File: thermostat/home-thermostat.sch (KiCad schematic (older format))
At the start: 38 parts, among them J1 Thermosthat, U3 LM2574M-5, U4 LD1117S33TR_SOT223, U5 AT24C512

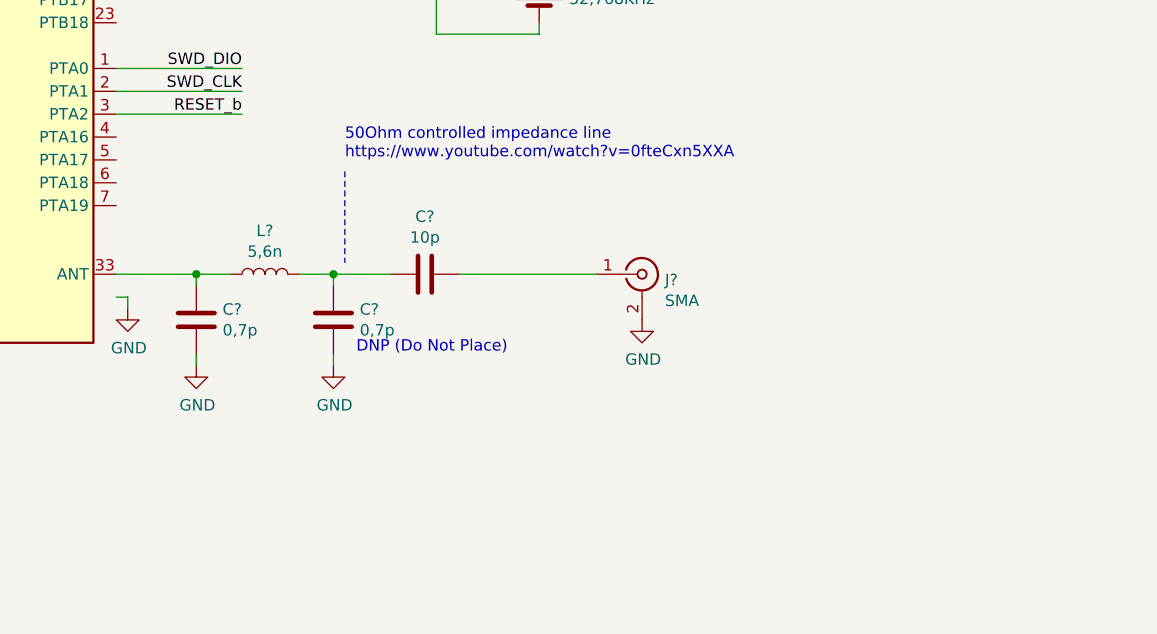
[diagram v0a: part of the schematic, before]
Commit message: Added some helpful comments to schematic, added explanation document to schematic of evalboard.
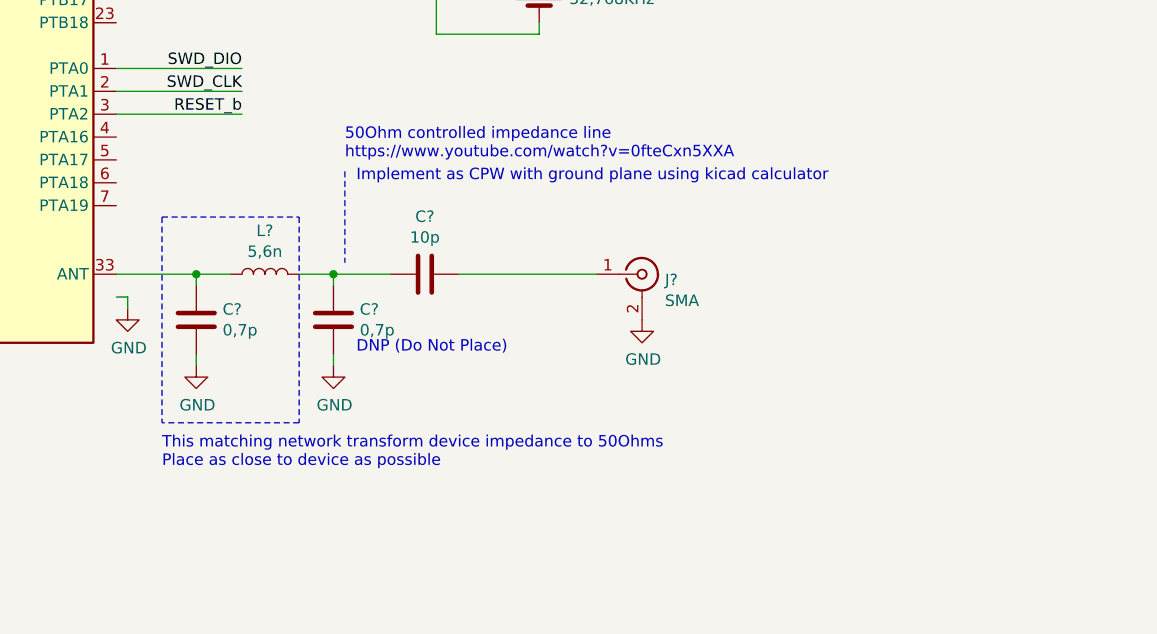
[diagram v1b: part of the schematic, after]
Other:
- note added: "Implement as CPW with ground plane using kicad calculator"
- note added: "This matching network transform device impedance to 50Ohms\nPlace as close to device as possible"
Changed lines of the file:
@@
 Wire Wire Line
 	7700 3800 8150 3800
+Text Notes 7350 4450 0    50   ~ 0
+Implement as CPW with ground plane using kicad calculator
+Wire Notes Line
+	6500 4600 7100 4600
+Wire Notes Line
+	7100 4600 7100 5500
+Wire Notes Line
+	7100 5500 6500 5500
+Wire Notes Line
+	6500 4600 6500 5500
+Text Notes 6500 5700 0    50   ~ 0
+This matching network transform device impedance to 50Ohms\nPlace as close to device as possible
 $EndSCHEMATC

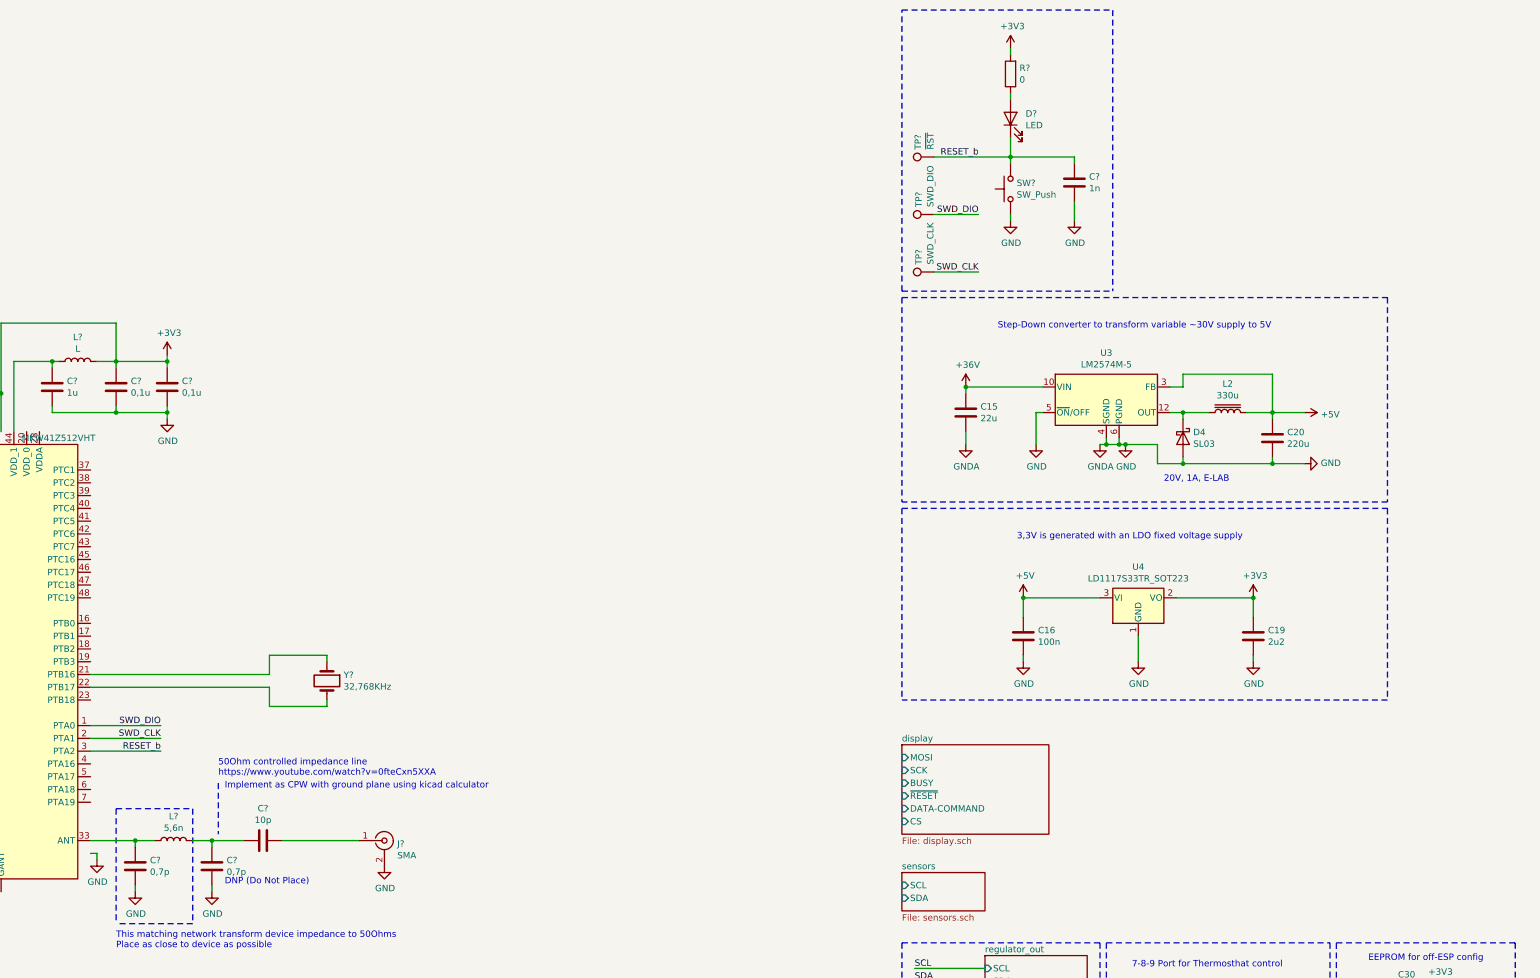
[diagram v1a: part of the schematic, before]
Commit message: Added some comments to pin usage on MKW41Z, reconfigured display to use 3 line SPI (no Data/Command pin) with 9 bit data packets
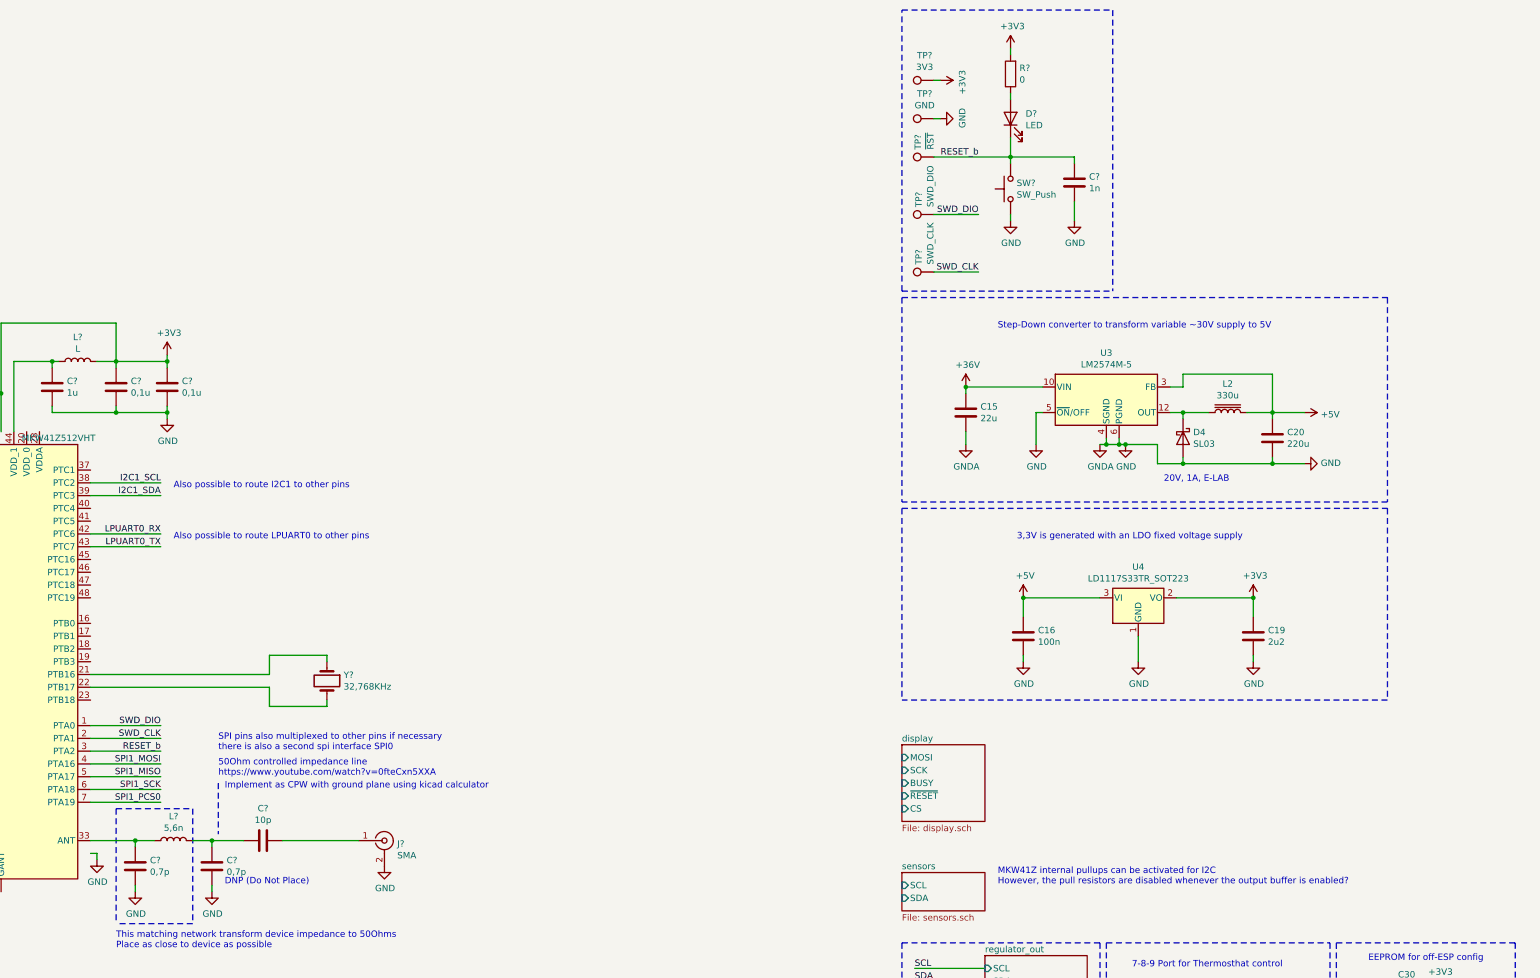
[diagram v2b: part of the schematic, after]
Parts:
- added TP?: GND, symbol Connector:TestPoint
- added TP?: 3V3, symbol Connector:TestPoint
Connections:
- net labels added: I2C1_SCL, I2C1_SDA, LPUART0_RX, LPUART0_TX, SPI1_MISO, SPI1_MOSI, SPI1_PCS0, SPI1_SCK
- wire segments 172 -> 182
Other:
- note added: "Also possible to route I2C1 to other pins"
- note added: "Also possible to route LPUART0 to other pins"
- note added: "MKW41Z internal pullups can be activated for I2C\nHowever, the pull resistors are disabled whenever the output buffer is enabled?"
- note added: "SPI pins also multiplexed to other pins if necessary\nthere is also a second spi interface SPI0"
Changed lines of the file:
@@
 Will we do peripherals with AVR or does MKW41Z has enough free pins?\nDo we want to try touch interface with MKW41 or AVR?
 $Sheet
-S 12650 4100 1150 700
+S 12650 4100 650  600
 U 5F306ECC
 F0 "display" 50
@@
 F4 "BUSY" I L 12650 4400 50
 F5 "~RESET" I L 12650 4500 50
-F6 "DATA-COMMAND" I L 12650 4600 50
-F7 "CS" I L 12650 4700 50
+F6 "CS" I L 12650 4600 50
 $EndSheet
 $Sheet
@@
 Text Notes 6500 5700 0    50   ~ 0
 This matching network transform device impedance to 50Ohms\nPlace as close to device as possible
+$Comp
+L Connector:TestPoint TP?
+U 1 1 5F554204
+P 12900 -800
+F 0 "TP?" V 13095 -728 50  0000 C CNN
+F 1 "GND" V 13004 -728 50  0000 C CNN
+F 2 "" H 13100 -800 50  0001 C CNN
+F 3 "~" H 13100 -800 50  0001 C CNN
+	1    12900 -800
+	0    -1   -1   0
+$EndComp
+$Comp
+L power:GND #PWR?
+U 1 1 5F5544E3
+P 12950 -800
+AR Path="/5E8AC4D3/5F5544E3" Ref="#PWR?"  Part="1"
+AR Path="/5F5544E3" Ref="#PWR?"  Part="1"
+F 0 "#PWR?" H 12950 -1050 50  0001 C CNN
+F 1 "GND" H 12955 -973 50  0000 C CNN
+F 2 "" H 12950 -800 50  0001 C CNN
+F 3 "" H 12950 -800 50  0001 C CNN
+	1    12950 -800
+	0    -1   -1   0
+$EndComp
+Wire Wire Line
+	12950 -800 12900 -800
+$Comp
+L power:+3V3 #PWR?
+U 1 1 5F55E07F
+P 12950 -1100
+AR Path="/5E8AC4D3/5F55E07F" Ref="#PWR?"  Part="1"
+AR Path="/5F55E07F" Ref="#PWR?"  Part="1"
+F 0 "#PWR?" H 12950 -1250 50  0001 C CNN
+F 1 "+3V3" H 12965 -927 50  0000 C CNN
+F 2 "" H 12950 -1100 50  0001 C CNN
+F 3 "" H 12950 -1100 50  0001 C CNN
+	1    12950 -1100
+	0    1    1    0
+$EndComp
+$Comp
+L Connector:TestPoint TP?
+U 1 1 5F55EE65
+P 12900 -1100
+F 0 "TP?" V 13095 -1028 50  0000 C CNN
+F 1 "3V3" V 13004 -1028 50  0000 C CNN
+F 2 "" H 13100 -1100 50  0001 C CNN
+F 3 "~" H 13100 -1100 50  0001 C CNN
+	1    12900 -1100
+	0    -1   -1   0
+$EndComp
+Wire Wire Line
+	12900 -1100 12950 -1100
+Text Label 6850 4250 2    50   ~ 0
+SPI1_MOSI
+Text Label 6850 4350 2    50   ~ 0
+SPI1_MISO
+Text Label 6850 4450 2    50   ~ 0
+SPI1_SCK
+Text Label 6850 4550 2    50   ~ 0
+SPI1_PCS0
+Wire Wire Line
+	6850 4250 6300 4250
+Wire Wire Line
+	6850 4350 6300 4350
+Wire Wire Line
+	6850 4450 6300 4450
+Wire Wire Line
+	6850 4550 6300 4550
+Text Notes 7300 4150 0    50   ~ 0
+SPI pins also multiplexed to other pins if necessary\nthere is also a second spi interface SPI0
+Text Notes 13400 5200 0    50   ~ 0
+MKW41Z internal pullups can be activated for I2C\nHowever, the pull resistors are disabled whenever the output buffer is enabled?
+Text Label 6850 2050 2    50   ~ 0
+I2C1_SCL
+Text Label 6850 2150 2    50   ~ 0
+I2C1_SDA
+Wire Wire Line
+	6850 2050 6300 2050
+Wire Wire Line
+	6850 2150 6300 2150
+Text Notes 6950 2100 0    50   ~ 0
+Also possible to route I2C1 to other pins
+Text Label 6850 2450 2    50   ~ 0
+LPUART0_RX
+Wire Wire Line
+	6850 2450 6300 2450
+Text Label 6850 2550 2    50   ~ 0
+LPUART0_TX
+Wire Wire Line
+	6850 2550 6300 2550
+Text Notes 6950 2500 0    50   ~ 0
+Also possible to route LPUART0 to other pins
 $EndSCHEMATC

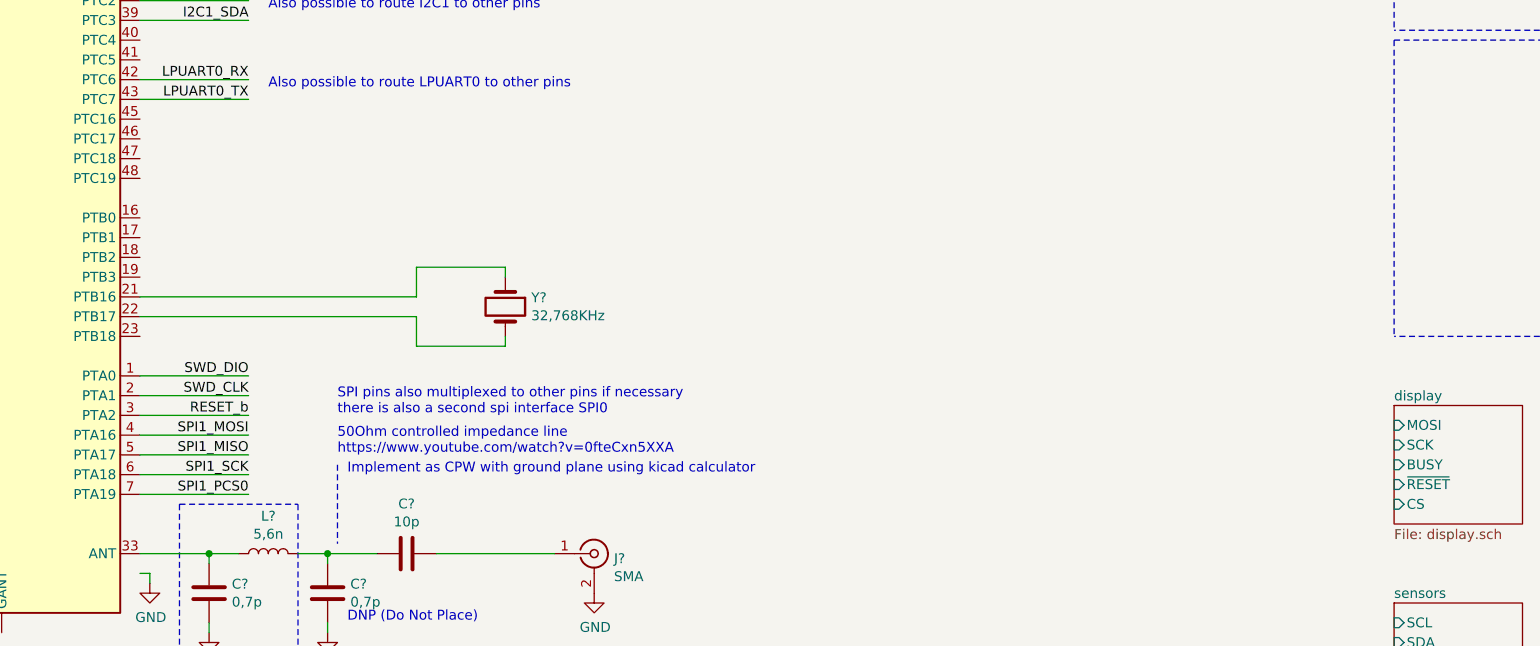
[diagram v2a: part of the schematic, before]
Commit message: Connected display SPI to MKW41Z
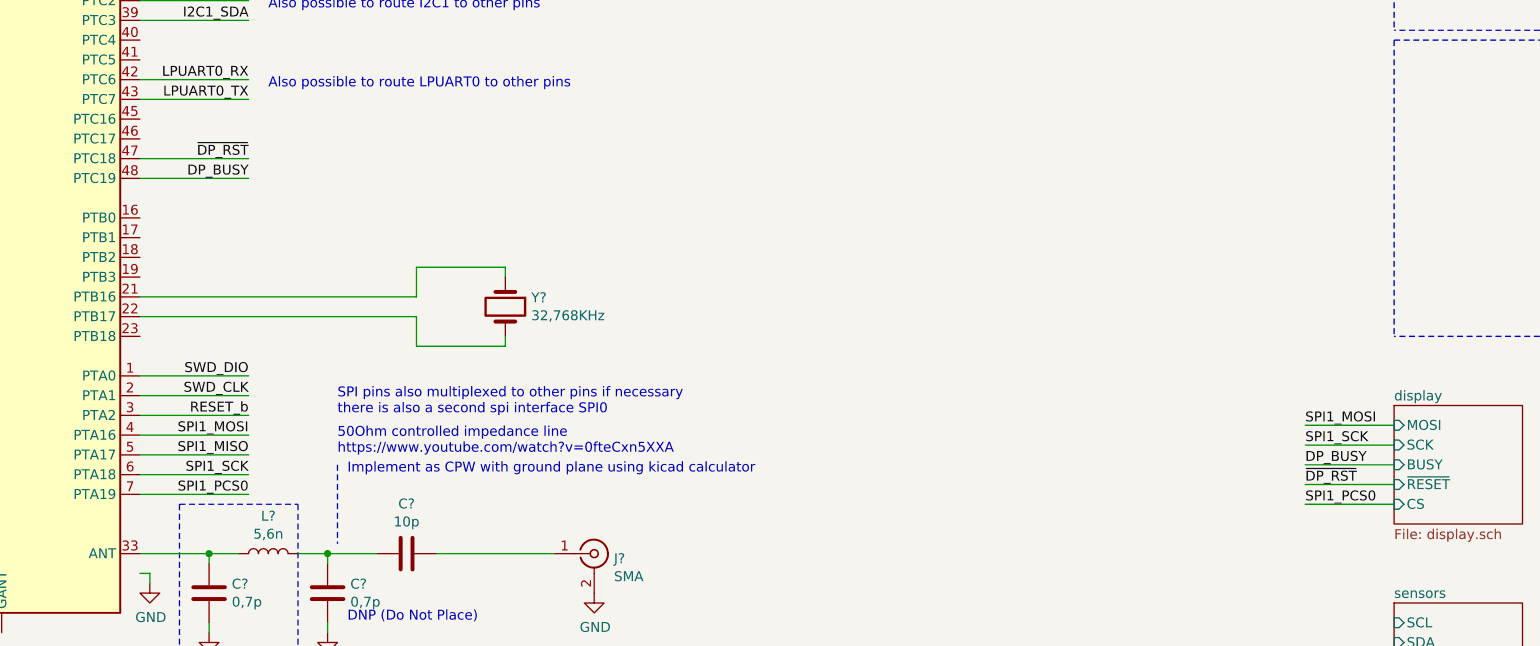
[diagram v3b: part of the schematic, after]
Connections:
- net labels added: DP_BUSY, ~DP_RST
- wire segments 182 -> 189
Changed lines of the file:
@@
 Text Notes 6950 2500 0    50   ~ 0
 Also possible to route LPUART0 to other pins
+Text Label 12200 4200 0    50   ~ 0
+SPI1_MOSI
+Text Label 12200 4300 0    50   ~ 0
+SPI1_SCK
+Text Label 12200 4600 0    50   ~ 0
+SPI1_PCS0
+Wire Wire Line
+	12200 4200 12650 4200
+Wire Wire Line
+	12200 4300 12650 4300
+Wire Wire Line
+	12200 4600 12650 4600
+Text Label 12200 4400 0    50   ~ 0
+DP_BUSY
+Wire Wire Line
+	12200 4400 12650 4400
+Wire Wire Line
+	12200 4500 12650 4500
+Text Label 12200 4500 0    50   ~ 0
+~DP_RST
+Text Label 6850 2950 2    50   ~ 0
+DP_BUSY
+Text Label 6850 2850 2    50   ~ 0
+~DP_RST
+Wire Wire Line
+	6850 2850 6300 2850
+Wire Wire Line
+	6850 2950 6300 2950
 $EndSCHEMATC
